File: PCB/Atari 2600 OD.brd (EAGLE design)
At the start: 58.5 x 61 mm, 16 parts, among them U1A SN74AHCT125N, U2A SN74AHCT125N, U3A SN74AHCT125N

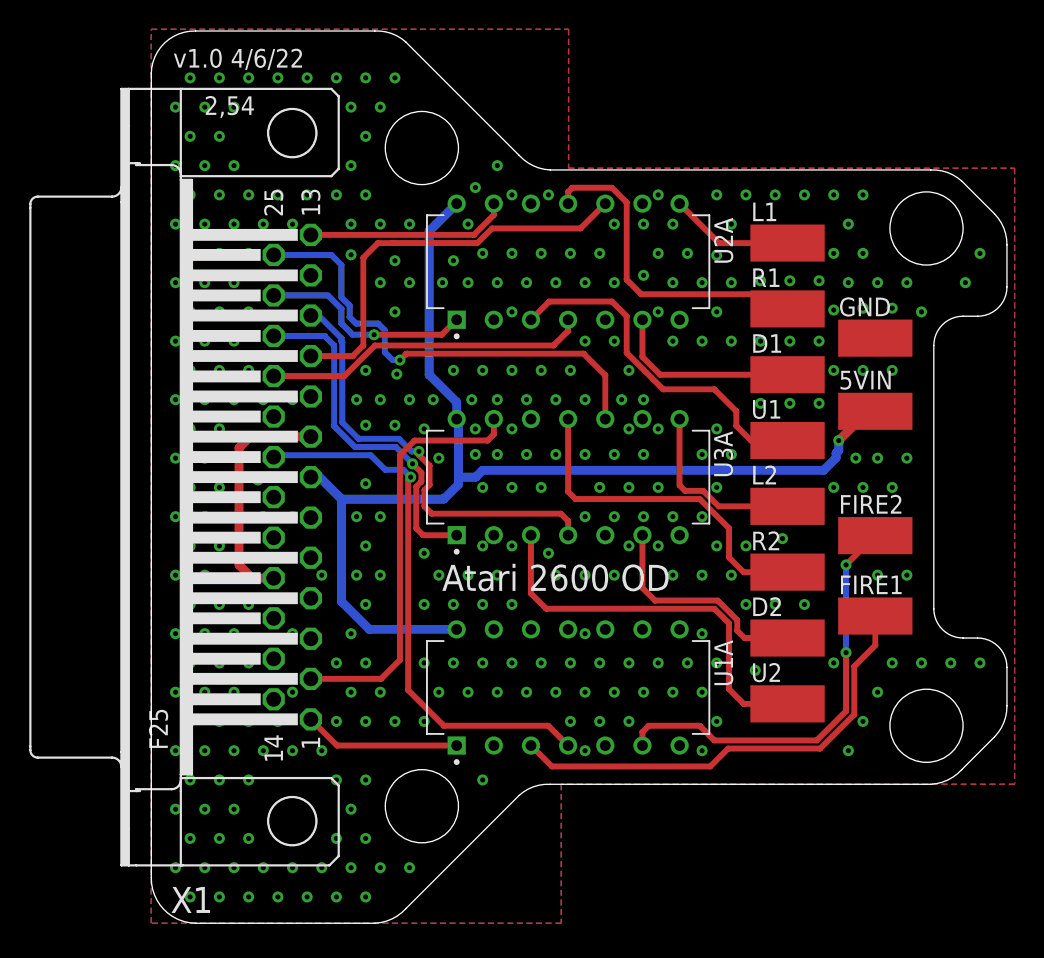
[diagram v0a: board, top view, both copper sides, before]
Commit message: Added exposed GND plane at DB25 anchors
All PCBs have been update to have exposed GND plane pads for the DB25 anchor points.

This resolves Issue 54
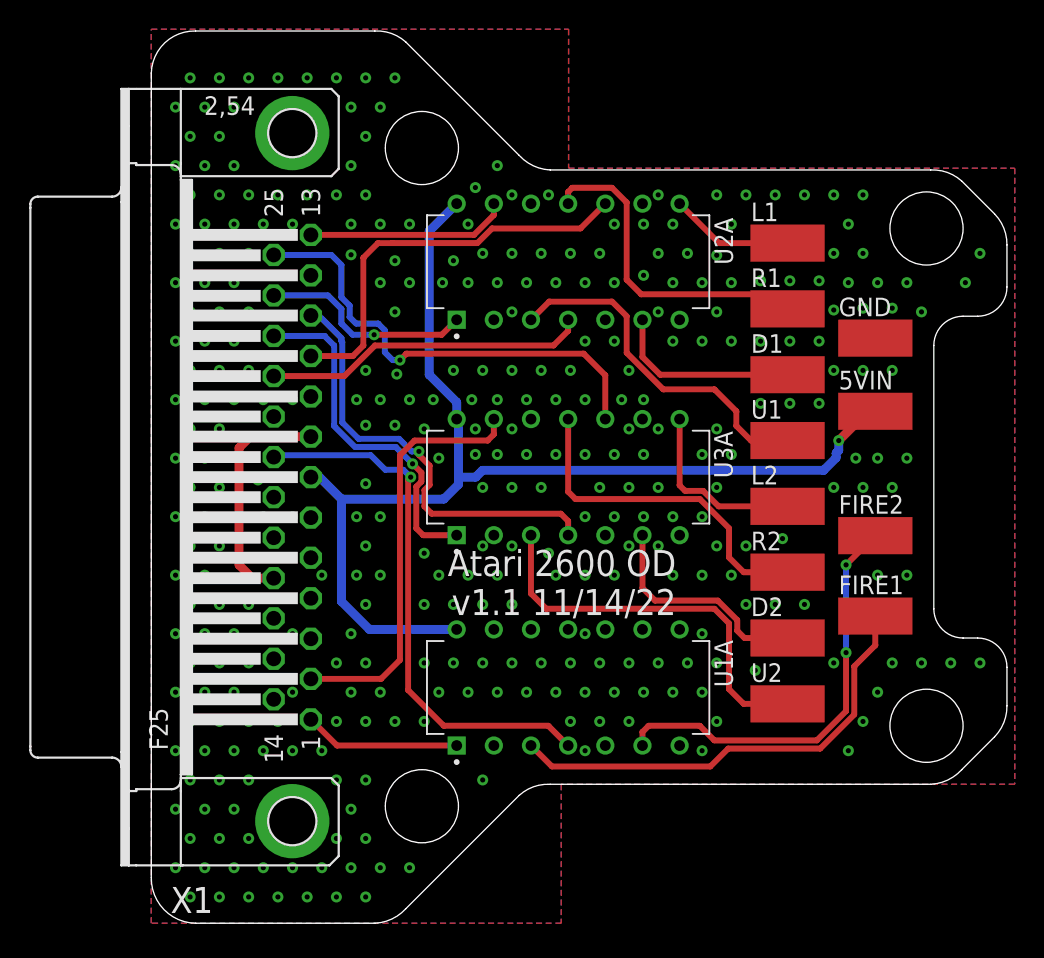
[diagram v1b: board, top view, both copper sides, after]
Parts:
- X1: device SparkFun-Retired:F25H -> SparkFun-Retired:F25HP
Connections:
- net GND: now also X1.GND1, X1.GND2
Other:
- board text added: "Atari 2600 OD v1.1 11/14/22"
- board text removed: "Atari 2600 OD"
- board text removed: "v1.0 4/6/22"
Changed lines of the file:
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@@
 <hole x="18.5" y="53" drill="5"/>
 <hole x="18.5" y="8" drill="5"/>
-<text x="1.5" y="58.5" size="1.27" layer="21">v1.0 4/6/22</text>
-<text x="35.5" y="24.5" size="1.778" layer="21" rot="R180">Atari 2600 OD</text>
+<text x="35.881" y="25.516" size="1.778" layer="21" rot="R180">Atari 2600 OD
+v1.1 11/14/22</text>
 <wire x1="58.5" y1="46.377359375" x2="58.5" y2="43.5" width="0" layer="20"/>
 <wire x1="58.5" y1="43.5" x2="56.5" y2="41.5" width="0" layer="20" curve="-90"/>
@@
 <attribute name="PURCHASE-URL" value="https://pricing.snapeda.com/search/part/SN74AHCT125N/?ref=eda" x="149.15" y="56.759" size="1.778" layer="27" rot="R90" display="off"/>
 </element>
-<element name="X1" library="SparkFun-Retired" package="F25H" value="" x="9.64" y="30.5" smashed="yes" rot="R90">
+<element name="X1" library="SparkFun-Retired" package="F25HP" value="" x="9.64" y="30.5" smashed="yes" rot="R90">
 <attribute name="NAME" x="4.219" y="2.48" size="1.778" layer="25" ratio="10" rot="R180"/>
 <attribute name="VALUE" x="-4.33" y="22.118" size="1.778" layer="27" ratio="10" rot="R90"/>
@@
 <contactref element="U2A" pad="7"/>
 <contactref element="GND" pad="1"/>
-<contactref element="X1" pad="9"/>
-<contactref element="X1" pad="6"/>
-<contactref element="X1" pad="5"/>
-<contactref element="X1" pad="4"/>
-<contactref element="X1" pad="16"/>
 <contactref element="U3A" pad="2"/>
 <contactref element="U3A" pad="5"/>
@@
 <contactref element="U1A" pad="10"/>
 <contactref element="U1A" pad="13"/>
-<contactref element="X1" pad="3"/>
 <via x="2.6568" y="1.7968" extent="1-16" drill="0.35"/>
 <via x="1.6568" y="3.7968" extent="1-16" drill="0.35"/>
@@
 <via x="55.6568" y="43.7968" extent="1-16" drill="0.35"/>
 <via x="56.6568" y="45.7968" extent="1-16" drill="0.35"/>
+<contactref element="X1" pad="GND1"/>
+<contactref element="X1" pad="GND2"/>
+<contactref element="X1" pad="9"/>
+<contactref element="X1" pad="6"/>
+<contactref element="X1" pad="5"/>
+<contactref element="X1" pad="4"/>
+<contactref element="X1" pad="16"/>
+<contactref element="X1" pad="3"/>
 </signal>
 <signal name="5VIN">
@@
 </drawing>
 <compatibility>
+<note version="6.3" minversion="6.2.2" severity="warning">
+Since Version 6.2.2 text objects can contain more than one line,
+which will not be processed correctly with this version.
+</note>
 <note version="8.2" severity="warning">
 Since Version 8.2, EAGLE supports online libraries. The ids

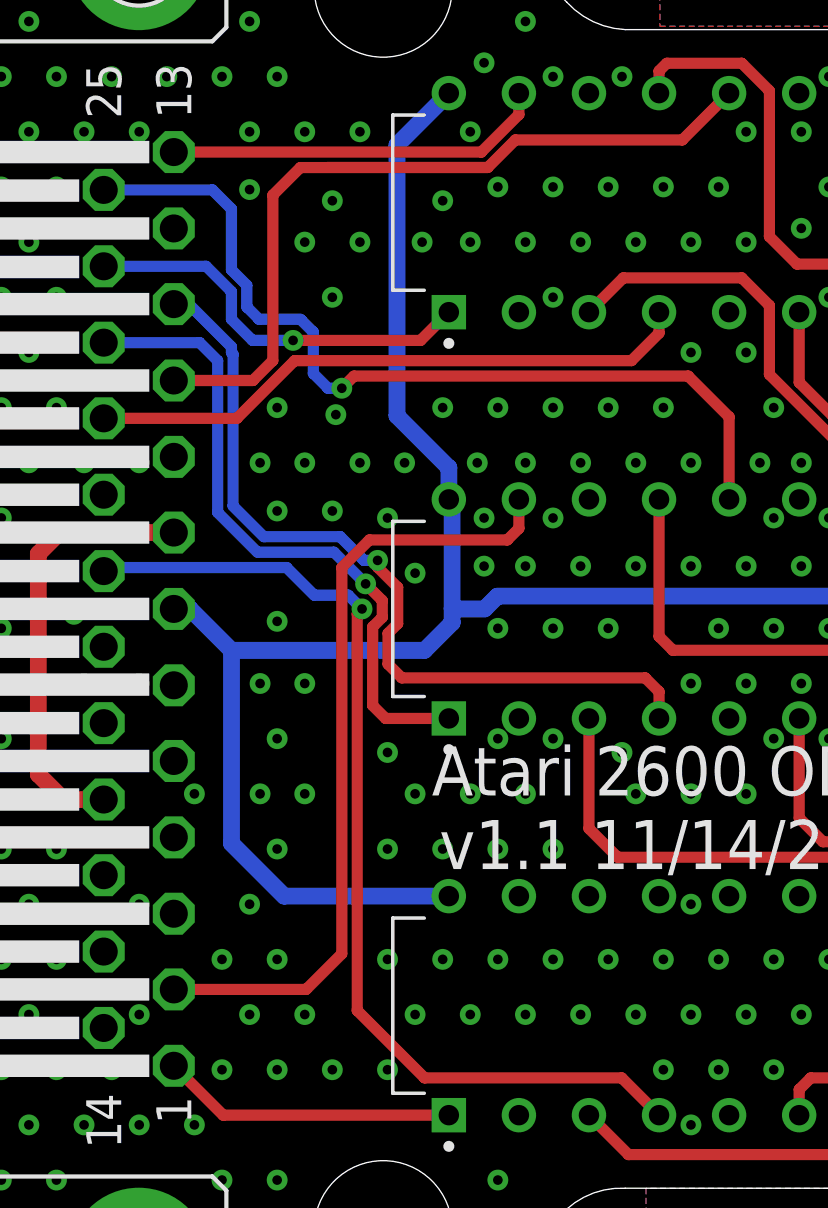
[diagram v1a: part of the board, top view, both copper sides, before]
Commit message: Silkscreen Update, Library Add, Datasheet Add
Updated the silkscreen on all PCBs that used the SN74 components as there was not orientation marker on the silkscreen.

Added Modified SN74 libraries and VB Cable Pinout image
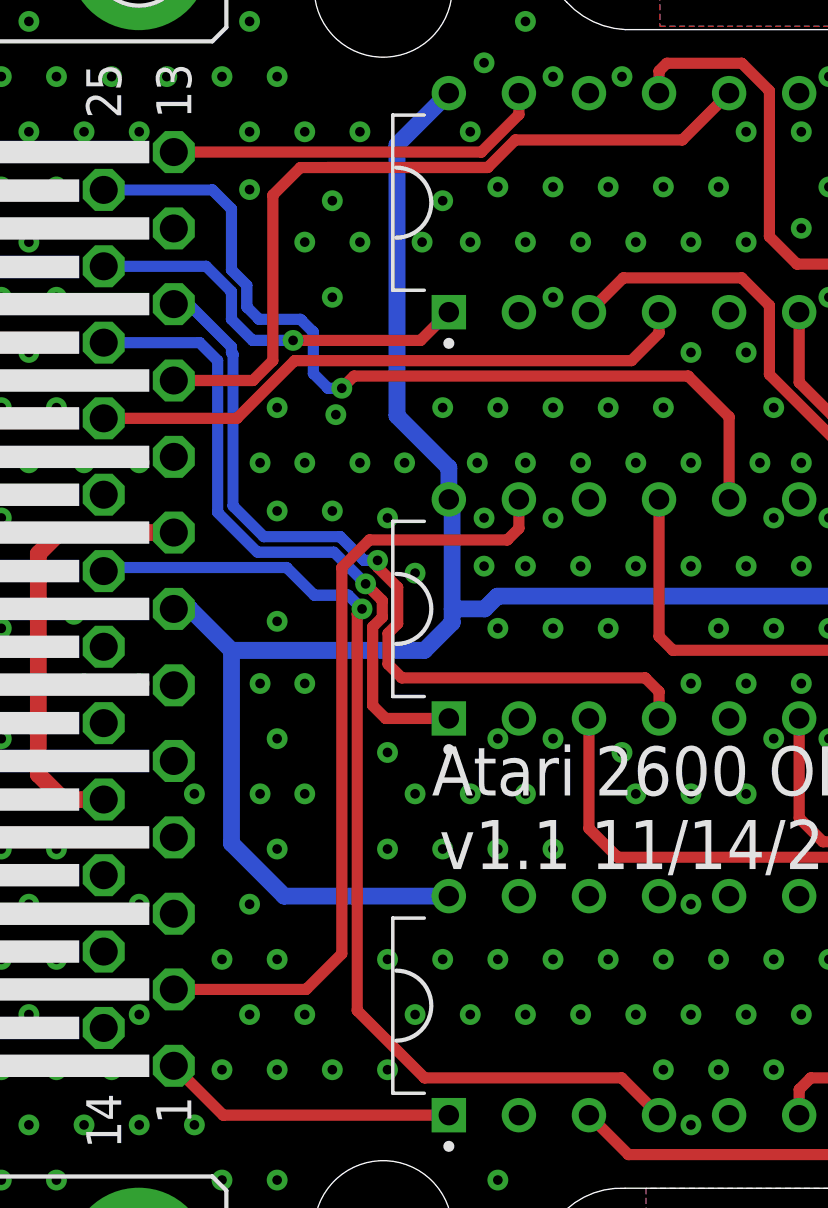
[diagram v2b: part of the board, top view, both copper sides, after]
